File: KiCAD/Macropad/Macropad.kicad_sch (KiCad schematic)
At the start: 1 part, among them U1 XIAO-RP2040-DIP

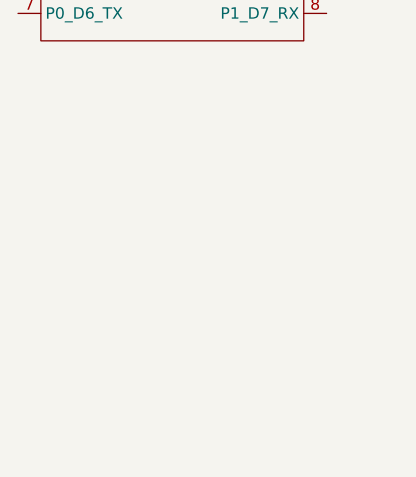
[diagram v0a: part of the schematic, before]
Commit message: Added roatary encoder and libraries.
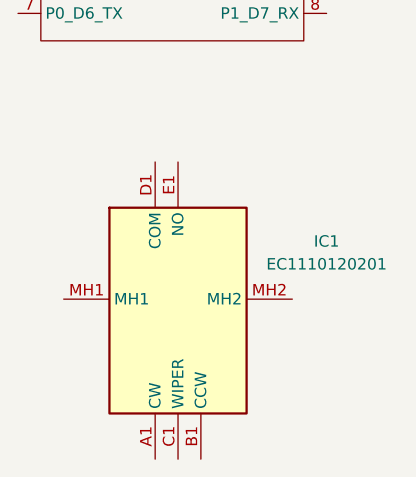
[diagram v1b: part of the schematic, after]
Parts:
- added IC1: EC1110120201, EC1110120201, symbol EC1110120201:EC1110120201
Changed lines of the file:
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@@
 	(paper "A4")
+	(symbol
+		(lib_id "EC1110120201:EC1110120201")
+		(at 222.25 134.62 0)
+		(unit 1)
+		(exclude_from_sim no)
+		(in_bom yes)
+		(on_board yes)
+		(dnp no)
+		(fields_autoplaced yes)
+		(property "Reference" "IC1"
+			(at 251.46 128.1998 0)
+			(effects
+				(font
+					(size 1.27 1.27)
+				)
+			)
+		)
+		(property "Value" "EC1110120201"
+			(at 251.46 130.7398 0)
+			(effects
+				(font
+					(size 1.27 1.27)
+				)
+			)
+		)
+		(property "Footprint" "EC1110120201"
+			(at 243.84 221.92 0)
+			(effects
+				(font
+					(size 1.27 1.27)
+				)
+				(justify left top)
+				(hide yes)
+			)
+		)
+		(property "Datasheet" "https://tech.alpsalpine.com/e/products/detail/EC1110120201/"
+			(at 243.84 321.92 0)
+			(effects
+				(font
+					(size 1.27 1.27)
+				)
+				(justify left top)
+				(hide yes)
+			)
+		)
+		(property "Description" "11mm Metal Shaft Type Encoder 5-Pin Tray - Trays"
+			(at 222.25 134.62 0)
+			(effects
+				(font
+					(size 1.27 1.27)
+				)
+				(hide yes)
+			)
+		)
+		(property "Height" "25"
+			(at 243.84 521.92 0)
+			(effects
+				(font
+					(size 1.27 1.27)
+				)
+				(justify left top)
+				(hide yes)
+			)
+		)
+		(property "Mouser Part Number" "688-EC1110120201"
+			(at 243.84 621.92 0)
+			(effects
+				(font
+					(size 1.27 1.27)
+				)
+				(justify left top)
+				(hide yes)
+			)
+		)
+		(property "Mouser Price/Stock" "https://www.mouser.co.uk/ProductDetail/Alps-Alpine/EC1110120201?qs=6EGMNY9ZYDQZuRRlni99ZQ%3D%3D"
+			(at 243.84 721.92 0)
+			(effects
+				(font
+					(size 1.27 1.27)
+				)
+				(justify left top)
+				(hide yes)
+			)
+		)
+		(property "Manufacturer_Name" "ALPS Electric"
+			(at 243.84 821.92 0)
+			(effects
+				(font
+					(size 1.27 1.27)
+				)
+				(justify left top)
+				(hide yes)
+			)
+		)
+		(property "Manufacturer_Part_Number" "EC1110120201"
+			(at 243.84 921.92 0)
+			(effects
+				(font
+					(size 1.27 1.27)
+				)
+				(justify left top)
+				(hide yes)
+			)
+		)
+		(pin "D1"
+		)
+		(pin "A1"
+		)
+		(pin "E1"
+		)
+		(pin "C1"
+		)
+		(pin "B1"
+		)
+		(pin "MH2"
+		)
+		(pin "MH1"
+		)
+		(instances
+			(project ""
+				(path "/50acfae0-7f10-4bf7-8da6-440d0ff2b716"
+					(reference "IC1")
+					(unit 1)
+				)
+			)
+		)
+	)
 	(symbol
 		(lib_id "Seeed_Studio_XIAO_Series:XIAO-RP2040-DIP")

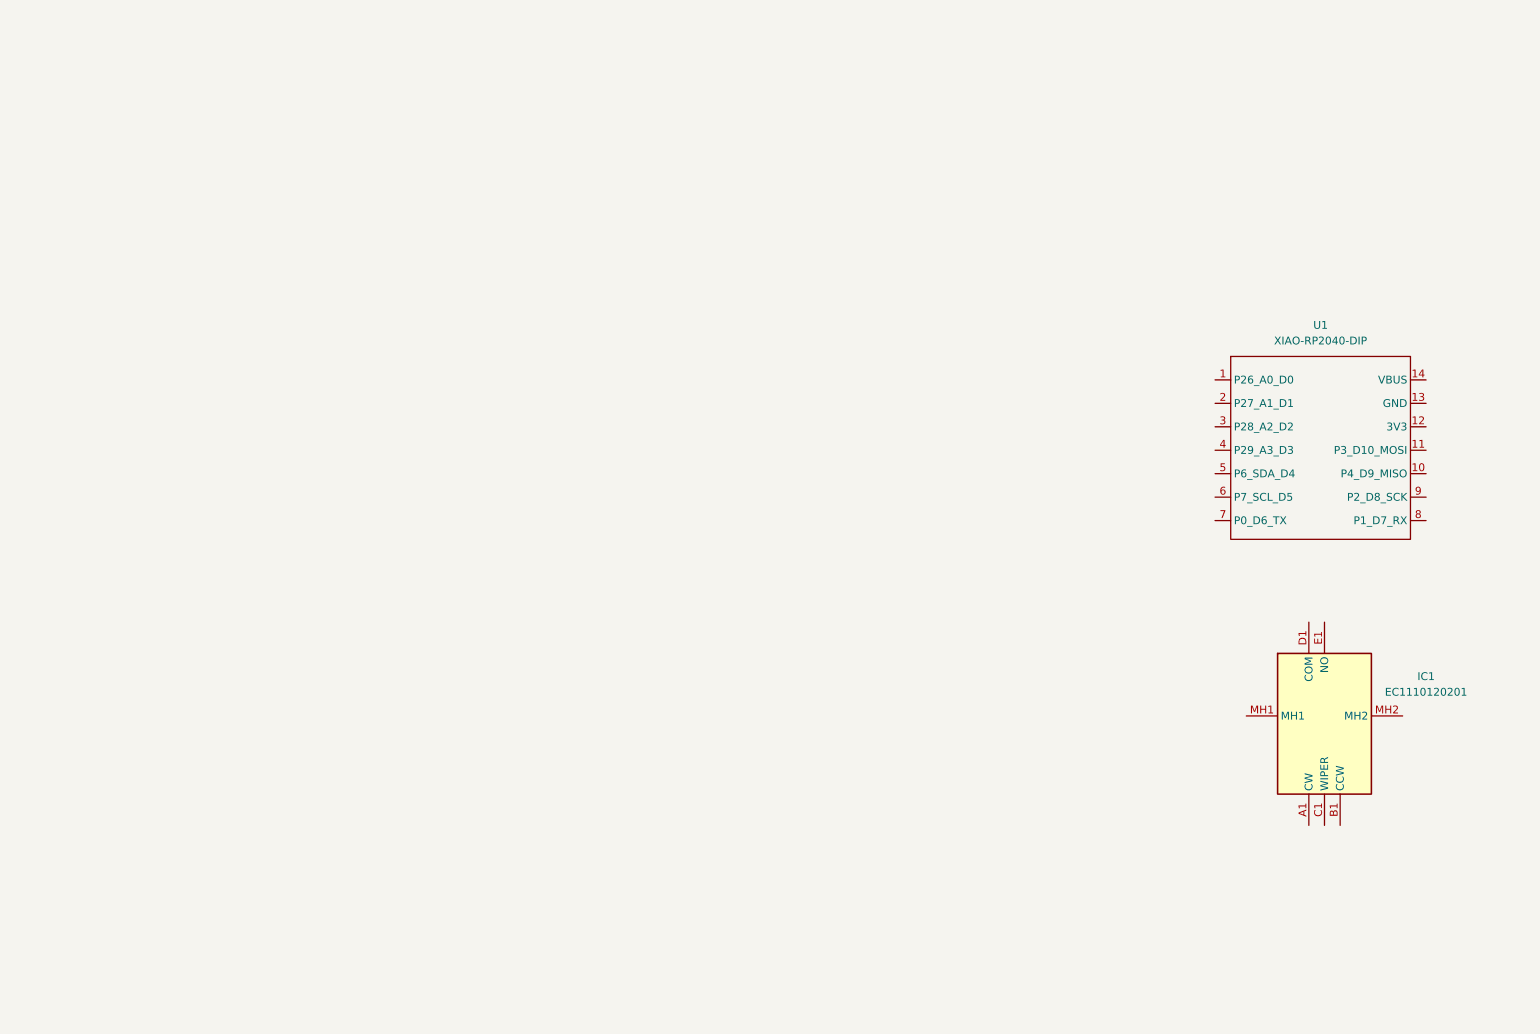
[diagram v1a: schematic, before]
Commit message: Updated schematic with push buttons and rotary encoder.
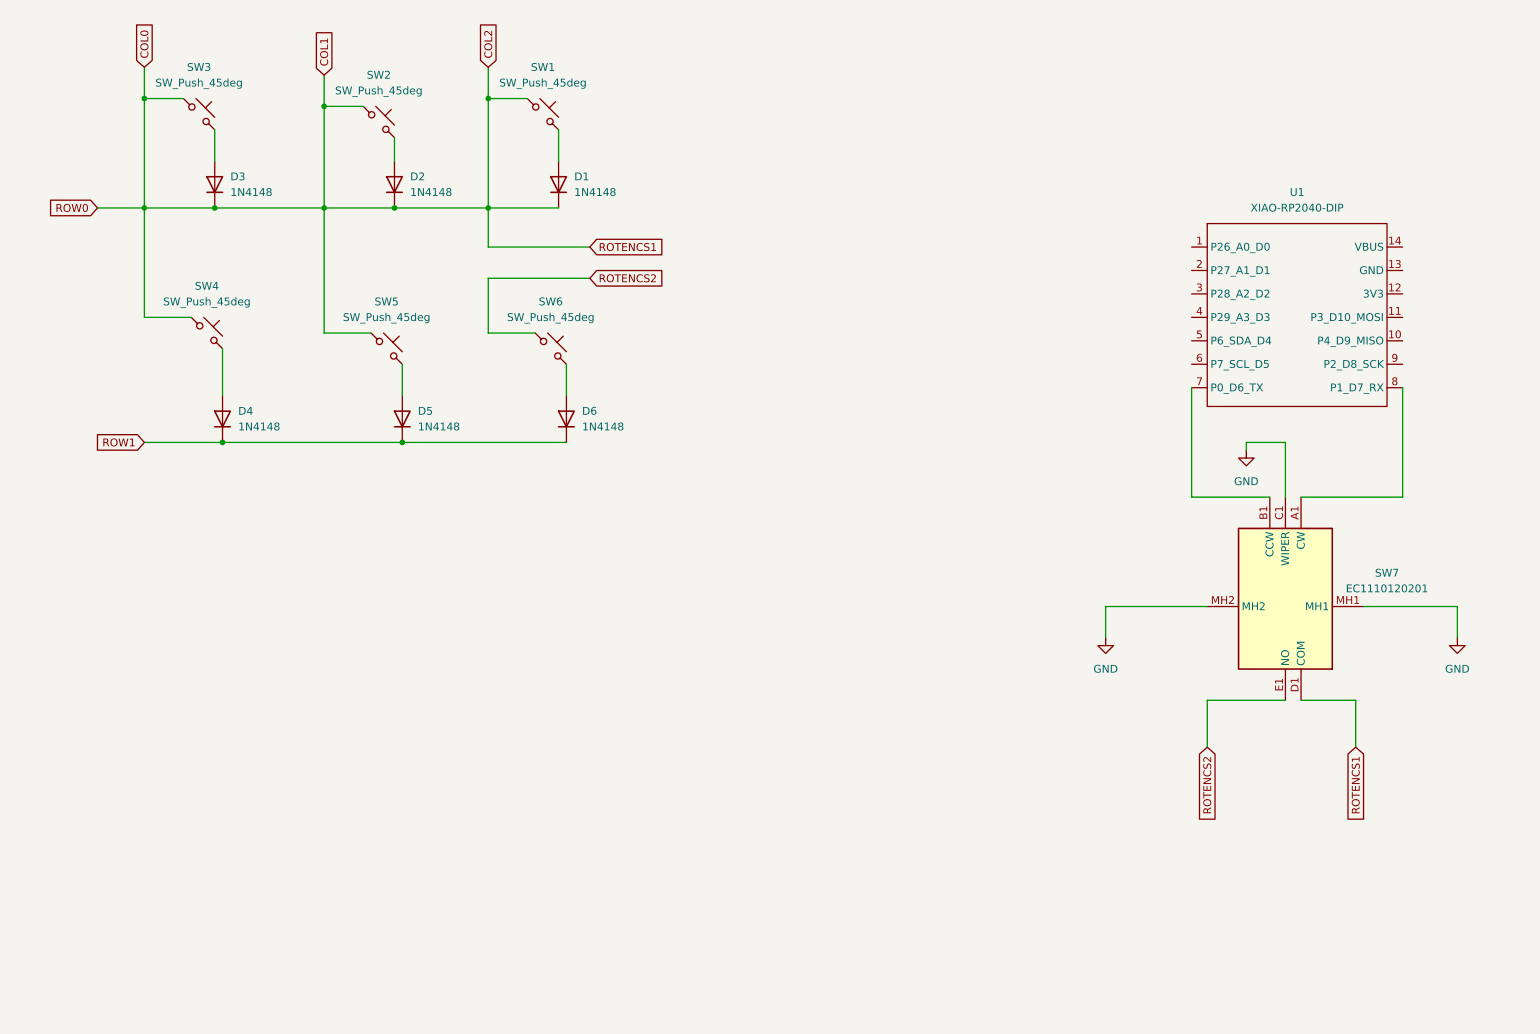
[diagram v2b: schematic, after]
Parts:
- removed IC1: EC1110120201, EC1110120201, symbol EC1110120201:EC1110120201
- added D1, D2, D3, D4, D5, D6: 1N4148, Diode_THT:D_DO-35_SOD27_P7.62mm_Horizontal, symbol Diode:1N4148
- added SW1, SW2, SW3, SW4, SW5, SW6: SW_Push_45deg, symbol Switch:SW_Push_45deg
- added SW7: EC1110120201, EC1110120201, symbol EC1110120201:EC1110120201
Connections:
- net at U1.7 (P0_D6_TX): now also SW7.B1 (CCW)
- net at U1.8 (P1_D7_RX): now also SW7.A1 (CW)
- new net: D3.2 (A), SW3.2
- new net: D2.2 (A), SW2.2
- new net: D4.2 (A), SW4.2
- new net: D1.2 (A), SW1.2
- new net: D6.2 (A), SW6.2
- new net: D5.2 (A), SW5.2
- new net COL0: D1.1 (K), D2.1 (K), D3.1 (K), SW1.1, SW2.1, SW3.1, SW4.1, SW5.1, SW7.D1 (COM)
- new net GND: SW7.C1 (WIPER), SW7.MH1, SW7.MH2
- new net ROTENCS2: SW6.1, SW7.E1 (NO)
- new net ROW1: D4.1 (K), D5.1 (K), D6.1 (K)
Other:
- moved on the sheet: U1

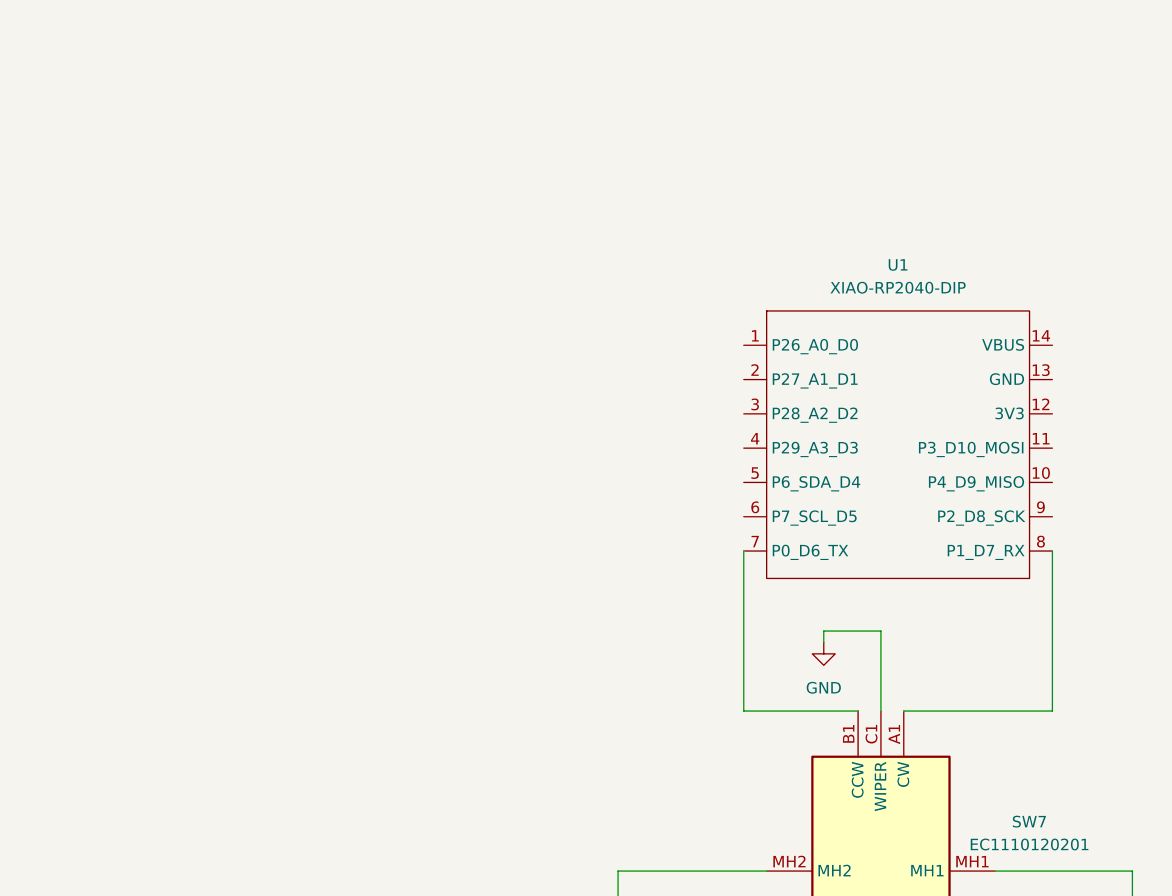
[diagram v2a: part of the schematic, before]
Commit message: Added majority of components to schematic. :)
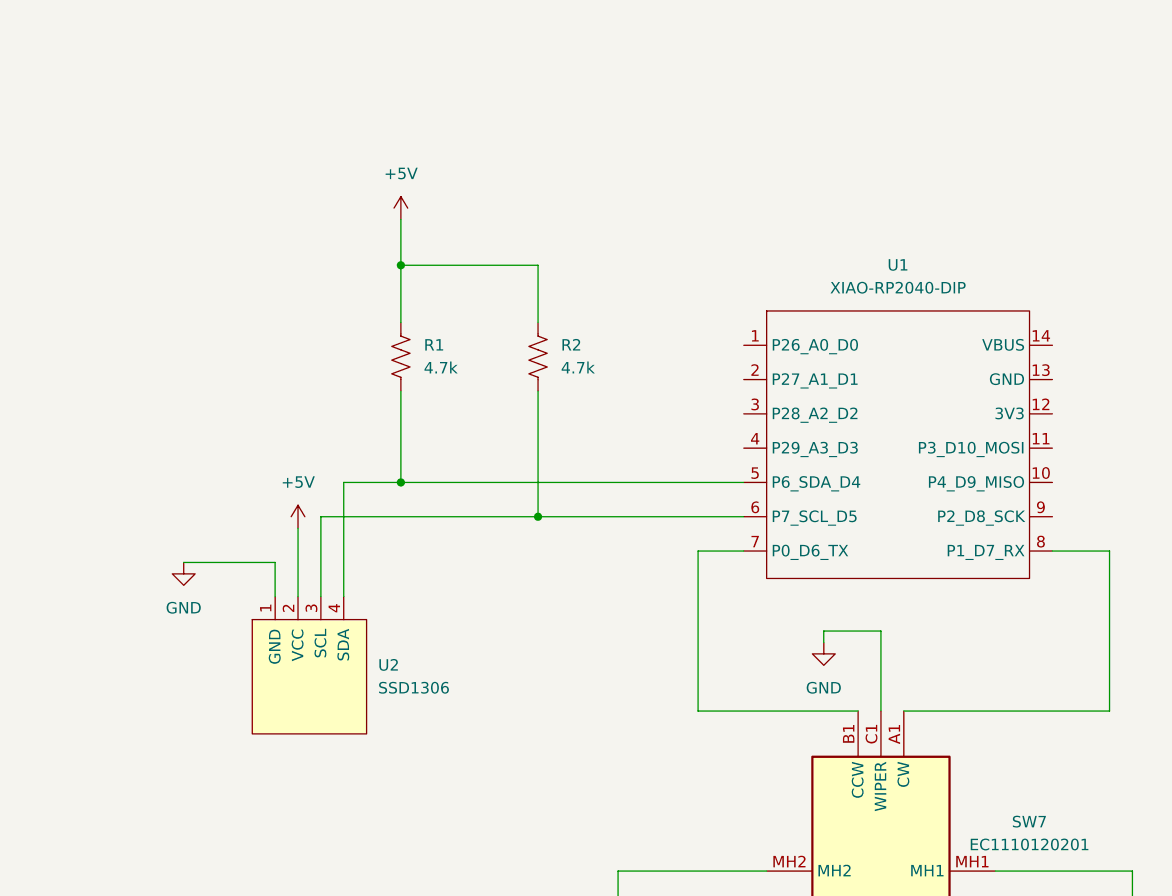
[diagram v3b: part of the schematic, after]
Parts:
- added R1, R2: 4.7k, Resistor_THT:R_Axial_DIN0207_L6.3mm_D2.5mm_P7.62mm_Horizontal, symbol Device:R_US
- added U2: SSD1306, DM-OLED096-636:MODULE_DM-OLED096-636, symbol SSD1306-128x64_OLED:SSD1306
- SW7: Mouser Part Number 688-EC1110120201 -> (none); Part_Number (none) -> 688-EC1110120201; Vendor (none) -> Mouser
- U1: Part_Number (none) -> https://www.amazon.com/Microcontroller-Dual-Core-MicroPytho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; Vendor (none) -> Amazon
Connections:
- net GND: now also U2.1 (GND)
- net at U1.5 (P6_SDA_D4): now also R1.1, U2.4 (SDA)
- net at U1.6 (P7_SCL_D5): now also R2.1, U2.3 (SCL)
- new net +5V: R1.2, R2.2, U2.2 (VCC)
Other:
- company: (none) -> Hamstersarus LLC
- title: (none) -> HackClub Macropad
